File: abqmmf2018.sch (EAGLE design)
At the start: 14 parts

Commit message: Moving Screen & Sensor, Remove ADC Resistor
Moving the Sensor more right since it's smaller than I had
somewhat expected, so that's nice.  Moved the screen so that
it's more inside the cloud.

Obviously had to do some rerouting to accomodate.  Like it a
little better anyway.

Also removed the ADC voltage divider resistor.  Turns out
you can muck with the boot firmware enough to flip the ADC
line to measure a 3.3V VDD value.  This seems to return about
2.9V with a full battery, and will go until it hits about
1.53V-ish before the NodeMCU just falls over.  Amusingly the
OLED screen (on my test) kept going.
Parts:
- removed R1: 420k, SparkFun-Resistors:1KOHM-HORIZ-1/4W-1%
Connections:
- net ADC: no longer R1.1
- net VCC: no longer R1.2
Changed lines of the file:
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@@
 <part name="U$4" library="microbuilder" deviceset="3.3V" device=""/>
 <part name="JP2" library="pinhead" deviceset="PINHD-2X10" device=""/>
-<part name="R1" library="SparkFun-Resistors" deviceset="1KOHM" device="-HORIZ-1/4W-1%" value="420k"/>
 </parts>
 <sheets>
@@
 <instance part="AMICA-NODEMCU" gate="G$1" x="38.1" y="180.34"/>
 <instance part="GND8" gate="1" x="15.24" y="154.94"/>
-<instance part="U$1" gate="G$1" x="78.74" y="193.04"/>
+<instance part="U$1" gate="G$1" x="78.74" y="205.74"/>
 <instance part="SUPPLY1" gate="G$1" x="5.08" y="203.2"/>
 <instance part="SUPPLY2" gate="G$1" x="20.32" y="251.46"/>
@@
 <instance part="U$4" gate="G$1" x="165.1" y="251.46"/>
 <instance part="JP2" gate="A" x="190.5" y="226.06"/>
-<instance part="R1" gate="G$1" x="35.56" y="231.14" rot="R90"/>
 </instances>
 <busses>
@@
 <pinref part="AMICA-NODEMCU" gate="G$1" pin="3V3@1"/>
 <wire x1="55.88" y1="185.42" x2="78.74" y2="185.42" width="0.1524" layer="91"/>
-<wire x1="78.74" y1="185.42" x2="78.74" y2="190.5" width="0.1524" layer="91"/>
+<wire x1="78.74" y1="185.42" x2="78.74" y2="203.2" width="0.1524" layer="91"/>
 <pinref part="U$1" gate="G$1" pin="3.3V"/>
 <pinref part="AMICA-NODEMCU" gate="G$1" pin="3V3@2"/>
@@
 <segment>
 <pinref part="AMICA-NODEMCU" gate="G$1" pin="RST"/>
-<wire x1="20.32" y1="167.64" x2="2.54" y2="167.64" width="0.1524" layer="91"/>
-<label x="2.54" y="167.64" size="1.778" layer="95"/>
+<wire x1="20.32" y1="167.64" x2="7.62" y2="167.64" width="0.1524" layer="91"/>
+<label x="7.62" y="167.64" size="1.778" layer="95"/>
 </segment>
 <segment>
@@
 <label x="172.72" y="226.06" size="1.778" layer="95"/>
 </segment>
-<segment>
-<pinref part="R1" gate="G$1" pin="1"/>
-<wire x1="35.56" y1="226.06" x2="35.56" y2="220.98" width="0.1524" layer="91"/>
-<wire x1="35.56" y1="220.98" x2="40.64" y2="220.98" width="0.1524" layer="91"/>
-<label x="38.1" y="220.98" size="1.778" layer="95"/>
-</segment>
 </net>
 <net name="GPIO16" class="0">
@@
 <segment>
 <pinref part="AMICA-NODEMCU" gate="G$1" pin="EN"/>
-<wire x1="20.32" y1="170.18" x2="2.54" y2="170.18" width="0.1524" layer="91"/>
-<label x="2.54" y="170.18" size="1.778" layer="95"/>
+<wire x1="20.32" y1="170.18" x2="7.62" y2="170.18" width="0.1524" layer="91"/>
+<label x="7.62" y="170.18" size="1.778" layer="95"/>
 </segment>
 <segment>
@@
 </segment>
 <segment>
+<pinref part="SUPPLY2" gate="G$1" pin="VCC"/>
 <pinref part="D1" gate="G$1" pin="C"/>
-<pinref part="SUPPLY2" gate="G$1" pin="VCC"/>
-<wire x1="20.32" y1="246.38" x2="20.32" y2="248.92" width="0.1524" layer="91"/>
-<wire x1="20.32" y1="248.92" x2="20.32" y2="251.46" width="0.1524" layer="91"/>
-<pinref part="R1" gate="G$1" pin="2"/>
-<wire x1="20.32" y1="248.92" x2="35.56" y2="248.92" width="0.1524" layer="91"/>
-<wire x1="35.56" y1="248.92" x2="35.56" y2="236.22" width="0.1524" layer="91"/>
-<junction x="20.32" y="248.92"/>
-</segment>
-<segment>
+<wire x1="20.32" y1="246.38" x2="20.32" y2="251.46" width="0.1524" layer="91"/>
+</segment>
+<segment>

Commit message: Button GPIO15 -> GPIO5
GPIO15 is apparently always pulled low due
to boot things (yay), so switching to GPIO5
to work around it.
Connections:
- net GPIO15: no longer S2.2
- net GPIO5/SCL: now also S2.2
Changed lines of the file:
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@@
-</segment>
-<segment>
-<wire x1="114.3" y1="248.92" x2="132.08" y2="248.92" width="0.1524" layer="91"/>
-<label x="119.38" y="248.92" size="1.778" layer="95"/>
-<pinref part="S2" gate="G$1" pin="2"/>
 </segment>
 <segment>
@@
 <pinref part="JP2" gate="A" pin="17"/>
 </segment>
+<segment>
+<wire x1="114.3" y1="248.92" x2="132.08" y2="248.92" width="0.1524" layer="91"/>
+<label x="119.38" y="248.92" size="1.778" layer="95"/>
+<pinref part="S2" gate="G$1" pin="2"/>
+</segment>
 </net>

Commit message: Removing Buttons for GPIO9/10
These are basically unusable on a certain portion of NodeMCUs,
so removing them entirely
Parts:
- removed S4, S5: MOMENTARY-SWITCH-SPST-PTH-6.0MM, SparkFun-Switches:MOMENTARY-SWITCH-SPST-PTH-6.0MM
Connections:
- net GND: no longer S4.1, S5.1
- net GPIO10: no longer S5.2
- net GPIO9: no longer S4.2
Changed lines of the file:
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@@
 <part name="U$2" library="microbuilder" deviceset="3.3V" device=""/>
 <part name="S1" library="SparkFun-Switches" deviceset="MOMENTARY-SWITCH-SPST" device="-PTH-6.0MM"/>
-<part name="S4" library="SparkFun-Switches" deviceset="MOMENTARY-SWITCH-SPST" device="-PTH-6.0MM"/>
-<part name="S5" library="SparkFun-Switches" deviceset="MOMENTARY-SWITCH-SPST" device="-PTH-6.0MM"/>
 <part name="U$3" library="Warthog9-Screens" deviceset="OLED-0.96" device="I2C-4PIN"/>
 <part name="GND1" library="supply1" deviceset="GND" device=""/>
@@
 <instance part="U$14" gate="G$1" x="55.88" y="256.54"/>
 <instance part="R10" gate="G$1" x="55.88" y="236.22" rot="R90"/>
-<instance part="GND5" gate="1" x="96.52" y="208.28"/>
+<instance part="GND5" gate="1" x="96.52" y="223.52"/>
 <instance part="S2" gate="G$1" x="109.22" y="248.92"/>
 <instance part="S3" gate="G$1" x="109.22" y="238.76"/>
@@
 <instance part="U$2" gate="G$1" x="17.78" y="205.74"/>
 <instance part="S1" gate="G$1" x="109.22" y="259.08"/>
-<instance part="S4" gate="G$1" x="109.22" y="228.6"/>
-<instance part="S5" gate="G$1" x="109.22" y="218.44"/>
 <instance part="U$3" gate="G$1" x="111.76" y="175.26"/>
 <instance part="GND1" gate="1" x="142.24" y="175.26"/>
@@
 <pinref part="S2" gate="G$1" pin="1"/>
 <wire x1="96.52" y1="248.92" x2="96.52" y2="238.76" width="0.1524" layer="91"/>
-<wire x1="96.52" y1="238.76" x2="96.52" y2="228.6" width="0.1524" layer="91"/>
-<wire x1="96.52" y1="228.6" x2="96.52" y2="218.44" width="0.1524" layer="91"/>
-<wire x1="96.52" y1="218.44" x2="96.52" y2="210.82" width="0.1524" layer="91"/>
+<wire x1="96.52" y1="238.76" x2="96.52" y2="226.06" width="0.1524" layer="91"/>
 <wire x1="104.14" y1="248.92" x2="96.52" y2="248.92" width="0.1524" layer="91"/>
 <junction x="96.52" y="248.92"/>
@@
 <wire x1="104.14" y1="238.76" x2="96.52" y2="238.76" width="0.1524" layer="91"/>
 <junction x="96.52" y="238.76"/>
-<pinref part="S4" gate="G$1" pin="1"/>
-<wire x1="104.14" y1="228.6" x2="96.52" y2="228.6" width="0.1524" layer="91"/>
-<junction x="96.52" y="228.6"/>
-<pinref part="S5" gate="G$1" pin="1"/>
-<wire x1="104.14" y1="218.44" x2="96.52" y2="218.44" width="0.1524" layer="91"/>
-<junction x="96.52" y="218.44"/>
 </segment>
 <segment>
@@
 </segment>
 <segment>
-<pinref part="S5" gate="G$1" pin="2"/>
-<wire x1="114.3" y1="218.44" x2="132.08" y2="218.44" width="0.1524" layer="91"/>
-<label x="119.38" y="218.44" size="1.778" layer="95"/>
-</segment>
-<segment>
 <wire x1="210.82" y1="231.14" x2="195.58" y2="231.14" width="0.1524" layer="91"/>
 <label x="205.74" y="231.14" size="1.778" layer="95"/>
@@
 </segment>
 <segment>
-<pinref part="S4" gate="G$1" pin="2"/>
-<wire x1="114.3" y1="228.6" x2="132.08" y2="228.6" width="0.1524" layer="91"/>
-<label x="119.38" y="228.6" size="1.778" layer="95"/>
-</segment>
-<segment>

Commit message: Removing GPIO9/10 from expansion header
These are unusable pins on enough NodeMCUs I'm going to go ahead
and remove the pins in the general sense
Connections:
- net GPIO10: no longer JP2.6
- net GPIO9: no longer JP2.19
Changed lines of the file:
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@@
 <pinref part="AMICA-NODEMCU" gate="G$1" pin="SD3"/>
-</segment>
-<segment>
-<wire x1="210.82" y1="231.14" x2="195.58" y2="231.14" width="0.1524" layer="91"/>
-<label x="205.74" y="231.14" size="1.778" layer="95"/>
-<pinref part="JP2" gate="A" pin="6"/>
 </segment>
 </net>
@@
 <pinref part="AMICA-NODEMCU" gate="G$1" pin="SD2"/>
 </segment>
-<segment>
-<wire x1="187.96" y1="213.36" x2="172.72" y2="213.36" width="0.1524" layer="91"/>
-<label x="172.72" y="213.36" size="1.778" layer="95"/>
-<pinref part="JP2" gate="A" pin="19"/>
-</segment>
 </net>

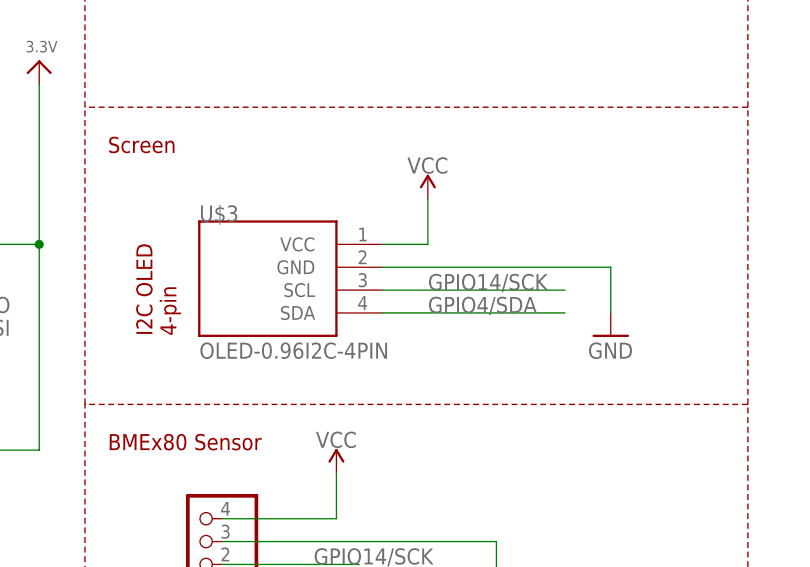
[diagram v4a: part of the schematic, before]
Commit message: Use the 0.96in OLED pinout that's got vcc/gnd reversed
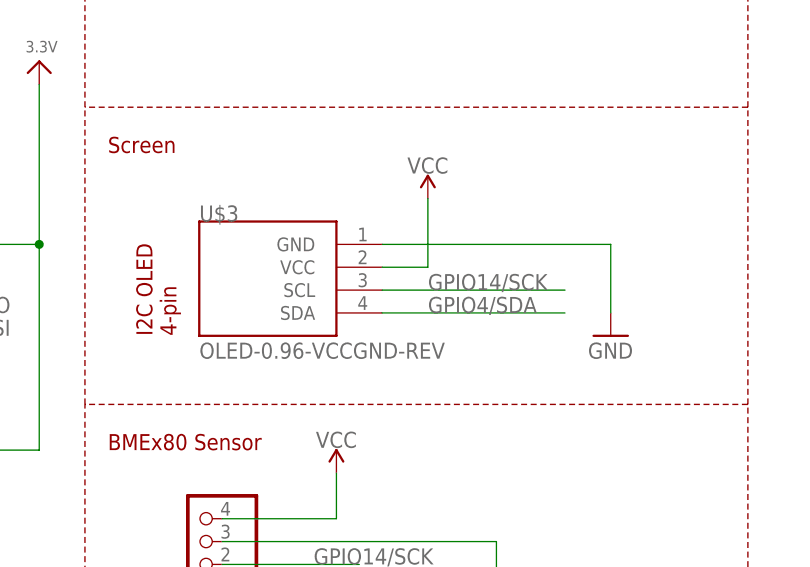
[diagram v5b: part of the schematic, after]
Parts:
- U$3: value OLED-0.96I2C-4PIN -> OLED-0.96-VCCGND-REV; device Warthog9-Screens:OLED-0.96I2C-4PIN -> Warthog9-Screens:OLED-0.96-VCCGND-REV
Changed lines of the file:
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@@
 <part name="U$2" library="microbuilder" deviceset="3.3V" device=""/>
 <part name="S1" library="SparkFun-Switches" deviceset="MOMENTARY-SWITCH-SPST" device="-PTH-6.0MM"/>
-<part name="U$3" library="Warthog9-Screens" deviceset="OLED-0.96" device="I2C-4PIN"/>
+<part name="U$3" library="Warthog9-Screens" deviceset="OLED-0.96-VCCGND-REV" device=""/>
 <part name="GND1" library="supply1" deviceset="GND" device=""/>
 <part name="JP1" library="pinhead" deviceset="PINHD-1X4" device=""/>
@@
 </segment>
 <segment>
-<pinref part="U$3" gate="G$1" pin="GND"/>
-<wire x1="116.84" y1="182.88" x2="142.24" y2="182.88" width="0.1524" layer="91"/>
-<wire x1="142.24" y1="182.88" x2="142.24" y2="177.8" width="0.1524" layer="91"/>
-<pinref part="GND1" gate="1" pin="GND"/>
-</segment>
-<segment>
 <pinref part="JP1" gate="A" pin="3"/>
 <pinref part="GND2" gate="1" pin="GND"/>
@@
 <junction x="170.18" y="228.6"/>
 </segment>
+<segment>
+<pinref part="U$3" gate="G$1" pin="GND"/>
+<pinref part="GND1" gate="1" pin="GND"/>
+<wire x1="116.84" y1="185.42" x2="142.24" y2="185.42" width="0.1524" layer="91"/>
+<wire x1="142.24" y1="185.42" x2="142.24" y2="177.8" width="0.1524" layer="91"/>
+</segment>
 </net>
 <net name="3.3V" class="0">
@@
 </segment>
 <segment>
-<pinref part="U$3" gate="G$1" pin="VCC"/>
-<wire x1="116.84" y1="185.42" x2="121.92" y2="185.42" width="0.1524" layer="91"/>
-<wire x1="121.92" y1="185.42" x2="121.92" y2="190.5" width="0.1524" layer="91"/>
-<pinref part="SUPPLY4" gate="G$1" pin="VCC"/>
-</segment>
-<segment>
 <pinref part="JP2" gate="A" pin="1"/>
 <pinref part="SUPPLY5" gate="G$1" pin="VCC"/>
@@
 <wire x1="172.72" y1="236.22" x2="172.72" y2="248.92" width="0.1524" layer="91"/>
 </segment>
-</net>
+<segment>
+<pinref part="U$3" gate="G$1" pin="VCC"/>
+<pinref part="SUPPLY4" gate="G$1" pin="VCC"/>
+<wire x1="116.84" y1="182.88" x2="121.92" y2="182.88" width="0.1524" layer="91"/>
+<wire x1="121.92" y1="182.88" x2="121.92" y2="190.5" width="0.1524" layer="91"/>
+</segment>
+</net>
